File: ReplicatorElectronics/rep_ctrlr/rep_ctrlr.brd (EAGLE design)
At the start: 106.5 x 89 mm, 98 parts, among them IC1 MICROCHIP_PIC32MX7X5F256L-PF, IC2 MICROCHIP_MCP6001-LT, IC3 MICROCHIP_MCP6001-LT, IC4 MICROCHIP_MCP6001-LT, IC5 MICROCHIP_MCP6001-LT, J1 ATX24RH, J10 SBH11-PBPC-D07-ST-BK, J11 SBH11-PBPC-D07-ST-BK, J12 SBH11-PBPC-D07-ST-BK, J13 SBH11-PBPC-D07-ST-BK, J14 SBH11-PBPC-D07-ST-BK, J15 SBH11-PBPC-D07-ST-BK, J16 SBH11-PBPC-D07-ST-BK, J17 SBH11-PBPC-D07-ST-BK, J18 SI-50170-F, J19 70553-0106, J4 RJ11-2L-B, J6 SBH11-PBPC-D05-ST-BK, J7 SBH11-PBPC-D05-ST-BK, J8 SBH11-PBPC-D05-ST-BK, J9 SBH11-PBPC-D05-ST-BK, Q1 ASFL1, Q2 ASFL1, U18 LDS3985XX33

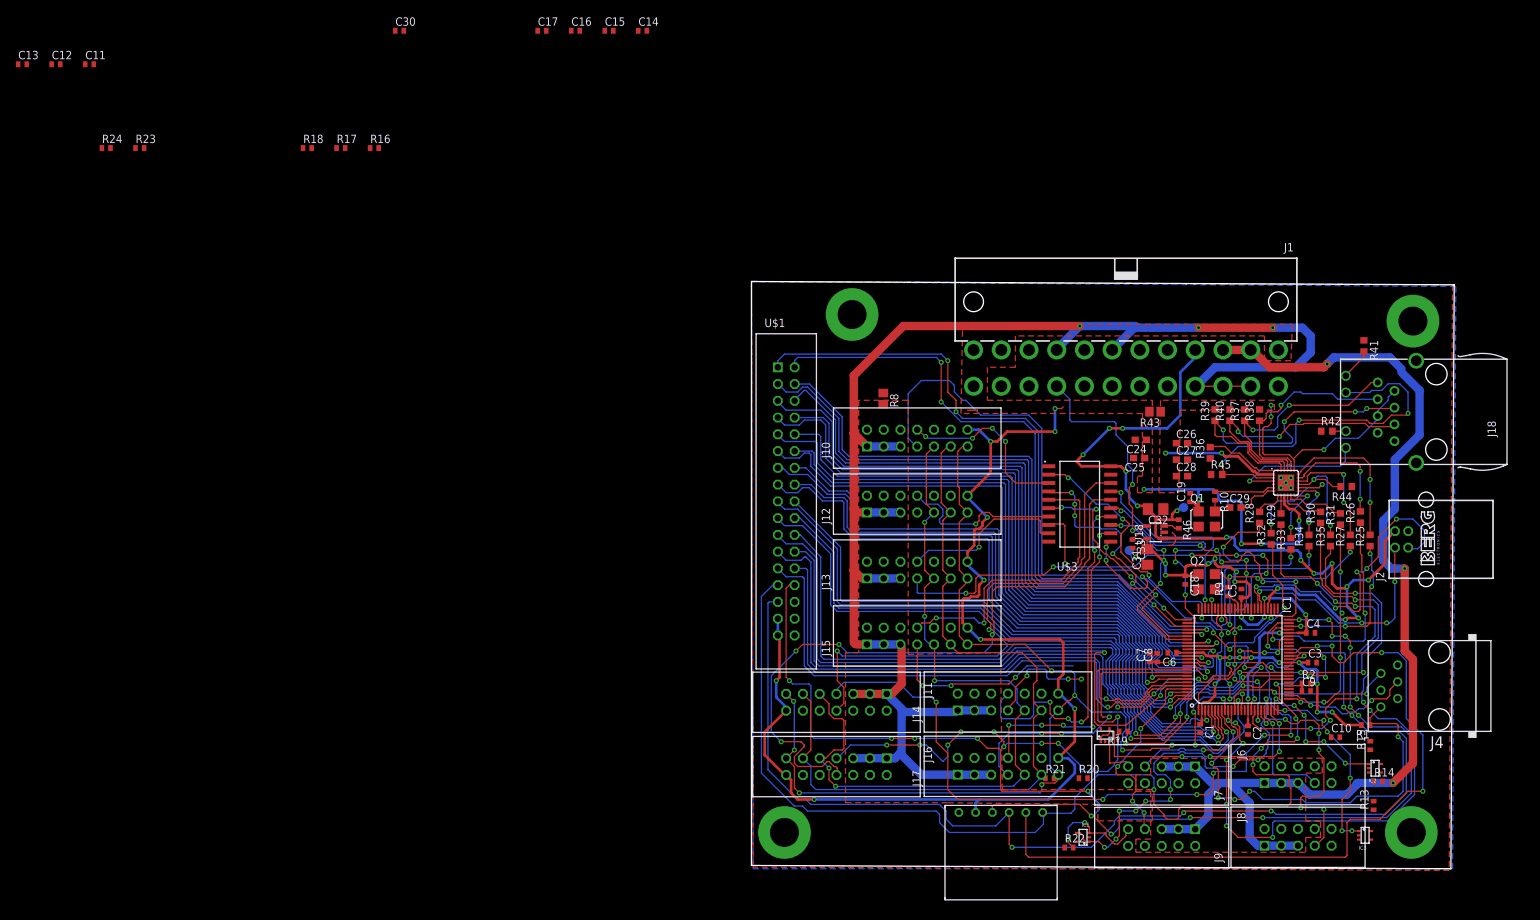
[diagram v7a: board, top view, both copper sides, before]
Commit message: 5/27/12: 3 PIC Pins remain (3 encoder CSN signals), as well as thermistor buffer routing at heater connectors. Pinswaps will be required on the PIC. DRC check reveals multiple conflicts which will require minor shifting around of traces overall after everything is connected.
~ 2 hrs.
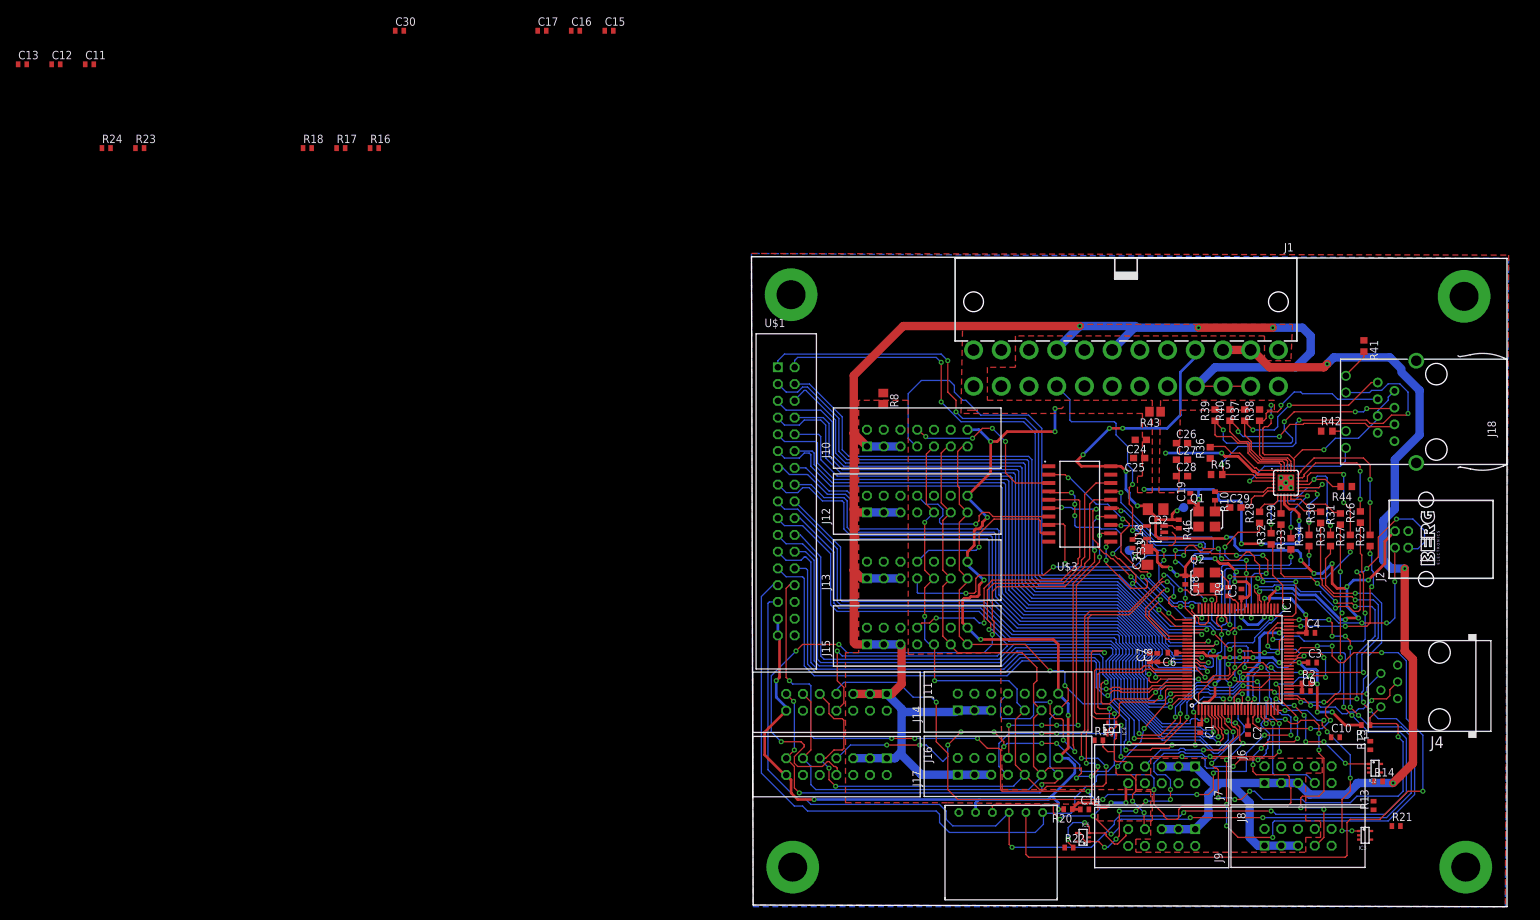
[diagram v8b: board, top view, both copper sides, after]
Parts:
- moved C14 135.7 mm to (50.5, 9.00)
- moved R21 53.0 mm to (97.7, 6.47)
- moved R20 5.23 mm to (48.0, 9.03), turned to 180 degrees
- moved R19 4.00 mm to (52.6, 19.5), turned to 0 degrees
- moved IC4 1.41 mm to (54.6, 21.2)
- moved Q2 0.25 mm to (69.0, 43.8)
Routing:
- net ENC_SCK: track 116.4 -> 184.7 mm, vias 5 -> 9
- net ENC_MOSI: track 117.6 -> 183.3 mm, vias 0 -> 8
- net ENC5_CSN: track 30.6 -> 0.00 mm, vias 3 -> 0
- net ENC4_CSN: track 16.8 -> 0.00 mm, vias 3 -> 0
- net N$17: track 0.00 -> 13.5 mm, vias 0 -> 2
- net SERVO4_5V: track 55.1 -> 62.6 mm
- net N$16: track 6.65 -> 9.67 mm
- net Y+: track 85.5 -> 82.7 mm
- net SERVO0: track 30.5 -> 33.1 mm
- net X+: track 82.7 -> 80.1 mm
- net ENC7_CSN: track 44.6 -> 47.1 mm
- net ENC3_CSN: track 71.3 -> 73.0 mm
- net SERVO7_5V: track 49.3 -> 47.7 mm
- net A0: track 110.9 -> 112.4 mm
- net SD_CSN: track 108.9 -> 110.1 mm
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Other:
- board size 106.5 x 89 mm -> 114.5 x 98.5 mm
